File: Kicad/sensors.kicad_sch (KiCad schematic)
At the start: 13 parts, among them J5 Conn_02x03_Top_Bottom, J6 Conn_02x03_Top_Bottom, J7 Conn_02x03_Top_Bottom, J8 Conn_02x03_Top_Bottom, U1 ITR8307, U2 ITR8307, U3 ITR8307

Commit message: not small changes
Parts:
- removed J6, J7, J8: Conn_02x03_Top_Bottom, Connector_PinSocket_2.54mm:PinSocket_2x03_P2.54mm_Vertical, symbol Connector_Generic:Conn_02x03_Top_Bottom
- added TF2, TF3, TF4: Conn_02x03_Top_Bottom, Connector_PinHeader_2.54mm:PinHeader_2x03_P2.54mm_Vertical, symbol Connector_Generic:Conn_02x03_Top_Bottom
- TF1: renamed from J5; footprint Connector_PinSocket_2.54mm:PinSocket_2x03_P2.54mm_Vertical -> Connector_PinHeader_2.54mm:PinHeader_2x03_P2.54mm_Vertical
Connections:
- net +3.3V: now also TF1.2 (Pin_2), TF2.2 (Pin_2), TF3.2 (Pin_2), TF4.2 (Pin_2); no longer TF1.1 (Pin_1)
- net EXTI1: now also TF1.5 (Pin_5); no longer TF1.6 (Pin_6)
- net EXTI2: now also TF2.5 (Pin_5)
- net EXTI3: now also TF3.5 (Pin_5)
- net EXTI4: now also TF4.5 (Pin_5)
- net GND: now also TF1.4 (Pin_4), TF2.4 (Pin_4), TF3.4 (Pin_4), TF4.4 (Pin_4); no longer TF1.3 (Pin_3)
- net SCL1: now also TF1.3 (Pin_3), TF2.3 (Pin_3); no longer TF1.4 (Pin_4)
- net SCL2: now also TF3.3 (Pin_3), TF4.3 (Pin_3)
- net SDA1: now also TF1.6 (Pin_6), TF2.6 (Pin_6); no longer TF1.5 (Pin_5)
- net SDA2: now also TF3.6 (Pin_6), TF4.6 (Pin_6)
- net XSHUT1: now also TF1.1 (Pin_1); no longer TF1.2 (Pin_2)
- net XSHUT2: now also TF2.1 (Pin_1)
- net XSHUT3: now also TF3.1 (Pin_1)
- net XSHUT4: now also TF4.1 (Pin_1)
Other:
- moved on the sheet: TF1

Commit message: fixed scheme with i2c
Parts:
- renumbered TF1 to ToF1
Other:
- moved on the sheet: TF3
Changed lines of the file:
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@@
 	(wire
 		(pts
-			(xy 115.57 110.49) (xy 119.38 110.49)
+			(xy 118.11 110.49) (xy 121.92 110.49)
 		)
 		(stroke
@@
 	(wire
 		(pts
-			(xy 115.57 107.95) (xy 132.08 107.95)
+			(xy 118.11 107.95) (xy 134.62 107.95)
 		)
 		(stroke
@@
 	(wire
 		(pts
-			(xy 100.33 107.95) (xy 102.87 107.95)
+			(xy 102.87 107.95) (xy 105.41 107.95)
 		)
 		(stroke
@@
 	(wire
 		(pts
-			(xy 132.08 107.95) (xy 132.08 110.49)
+			(xy 134.62 107.95) (xy 134.62 110.49)
 		)
 		(stroke
@@
 	(wire
 		(pts
-			(xy 99.06 113.03) (xy 102.87 113.03)
+			(xy 101.6 113.03) (xy 105.41 113.03)
 		)
 		(stroke
@@
 	(wire
 		(pts
-			(xy 87.63 110.49) (xy 87.63 109.22)
+			(xy 90.17 110.49) (xy 90.17 109.22)
 		)
 		(stroke
@@
 	(wire
 		(pts
-			(xy 115.57 113.03) (xy 118.11 113.03)
+			(xy 118.11 113.03) (xy 120.65 113.03)
 		)
 		(stroke
@@
 	(wire
 		(pts
-			(xy 102.87 110.49) (xy 87.63 110.49)
+			(xy 105.41 110.49) (xy 90.17 110.49)
 		)
 		(stroke
@@
 	(hierarchical_label "SCL2"
 		(shape input)
-		(at 99.06 113.03 180)
+		(at 101.6 113.03 180)
 		(effects
 			(font
@@
 	(hierarchical_label "XSHUT3"
 		(shape input)
-		(at 100.33 107.95 180)
+		(at 102.87 107.95 180)
 		(effects
 			(font
@@
 	(hierarchical_label "EXTI3"
 		(shape input)
-		(at 119.38 110.49 0)
+		(at 121.92 110.49 0)
 		(effects
 			(font
@@
 	(hierarchical_label "SDA2"
 		(shape bidirectional)
-		(at 118.11 113.03 0)
+		(at 120.65 113.03 0)
 		(effects
 			(font
@@
 	(symbol
 		(lib_id "power:GND")
-		(at 132.08 110.49 0)
+		(at 134.62 110.49 0)
 		(unit 1)
 		(exclude_from_sim no)
@@
 		(fields_autoplaced yes)
 		(property "Reference" "#PWR063"
-			(at 132.08 116.84 0)
+			(at 134.62 116.84 0)
 			(effects
 				(font
@@
 		)
 		(property "Value" "GND"
-			(at 132.08 115.57 0)
+			(at 134.62 115.57 0)
 			(effects
 				(font
@@
 		)
 		(property "Footprint" ""
-			(at 132.08 110.49 0)
+			(at 134.62 110.49 0)
 			(effects
 				(font
@@
 		)
 		(property "Datasheet" ""
-			(at 132.08 110.49 0)
+			(at 134.62 110.49 0)
 			(effects
 				(font
@@
 		)
 		(property "Description" "Power symbol creates a global label with name \"GND\" , ground"
-			(at 132.08 110.49 0)
+			(at 134.62 110.49 0)
 			(effects
 				(font
@@
 	(symbol
 		(lib_id "power:+3.3V")
-		(at 87.63 109.22 0)
+		(at 90.17 109.22 0)
 		(unit 1)
 		(exclude_from_sim no)
@@
 		(fields_autoplaced yes)
 		(property "Reference" "#PWR062"
-			(at 87.63 113.03 0)
+			(at 90.17 113.03 0)
 			(effects
 				(font
@@
 		)
 		(property "Value" "+3.3V"
-			(at 87.63 104.14 0)
+			(at 90.17 104.14 0)
 			(effects
 				(font
@@
 		)
 		(property "Footprint" ""
-			(at 87.63 109.22 0)
+			(at 90.17 109.22 0)
 			(effects
 				(font
@@
 		)
 		(property "Datasheet" ""
-			(at 87.63 109.22 0)
+			(at 90.17 109.22 0)
 			(effects
 				(font
@@
 		)
 		(property "Description" "Power symbol creates a global label with name \"+3.3V\""
-			(at 87.63 109.22 0)
+			(at 90.17 109.22 0)
 			(effects
 				(font
@@
 		(dnp no)
 		(fields_autoplaced yes)
-		(property "Reference" "TF1"
+		(property "Reference" "ToF1"
 			(at 59.69 102.87 0)
 			(effects
@@
 			(project "MiniSumoSTM"
 				(path "/74ccf643-7ae0-4d9b-8b7c-e7e124cb3f26/07b86d8b-af43-4da9-8375-8e0423139cdc"
-					(reference "TF1")
+					(reference "ToF1")
 					(unit 1)
 				)
@@
 	(symbol
 		(lib_id "Connector_Generic:Conn_02x03_Top_Bottom")
-		(at 107.95 110.49 0)
+		(at 110.49 110.49 0)
 		(unit 1)
 		(exclude_from_sim no)
@@
 		(fields_autoplaced yes)
 		(property "Reference" "TF3"
-			(at 109.22 104.14 0)
+			(at 111.76 104.14 0)
 			(effects
 				(font
@@
 		)
 		(property "Value" "Conn_02x03_Top_Bottom"
-			(at 109.22 104.14 0)
+			(at 111.76 104.14 0)
 			(effects
 				(font
@@
 		)
 		(property "Footprint" "Connector_PinHeader_2.54mm:PinHeader_2x03_P2.54mm_Vertical"
-			(at 107.95 110.49 0)
+			(at 110.49 110.49 0)
 			(effects
 				(font
@@
 		)
 		(property "Datasheet" "~"
-			(at 107.95 110.49 0)
+			(at 110.49 110.49 0)
 			(effects
 				(font
@@
 		)
 		(property "Description" "Generic connector, double row, 02x03, top/bottom pin numbering scheme (row 1: 1...pins_per_row, row2: pins_per_row+1 ... num_pins), script generated (kicad-library-utils/schlib/autogen/connector/)"
-			(at 107.95 110.49 0)
-			(effects
-				(font
+			(at 110.49 110.49 0)
+			(effects
+				(font

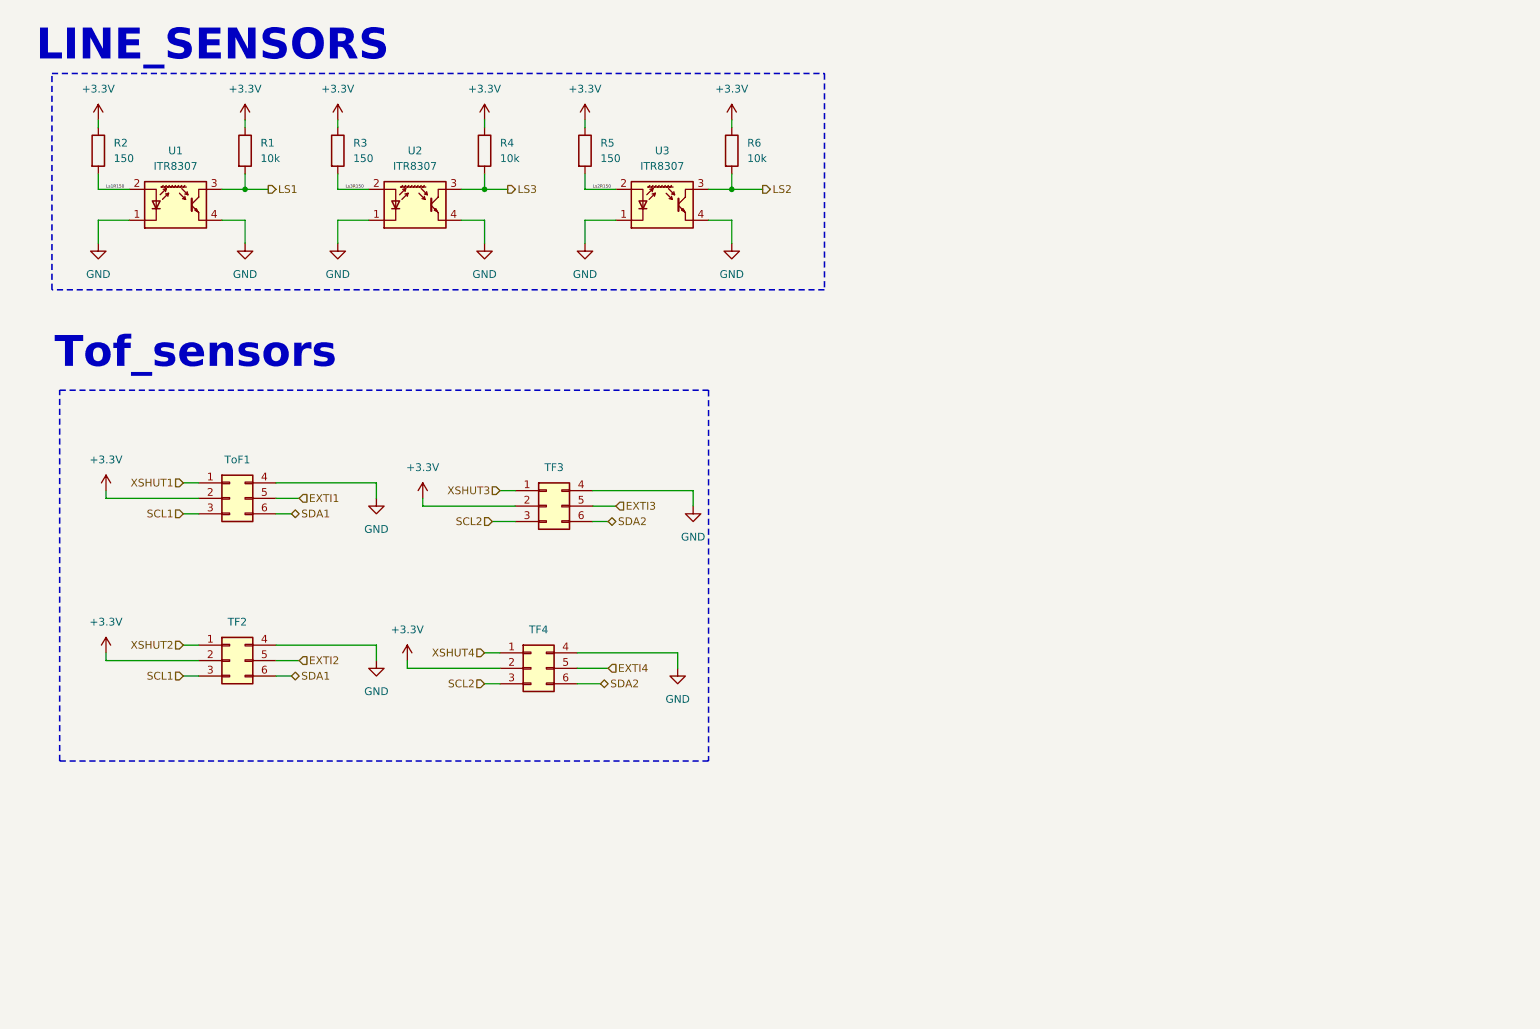
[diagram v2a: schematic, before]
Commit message: kicad schemas documentation
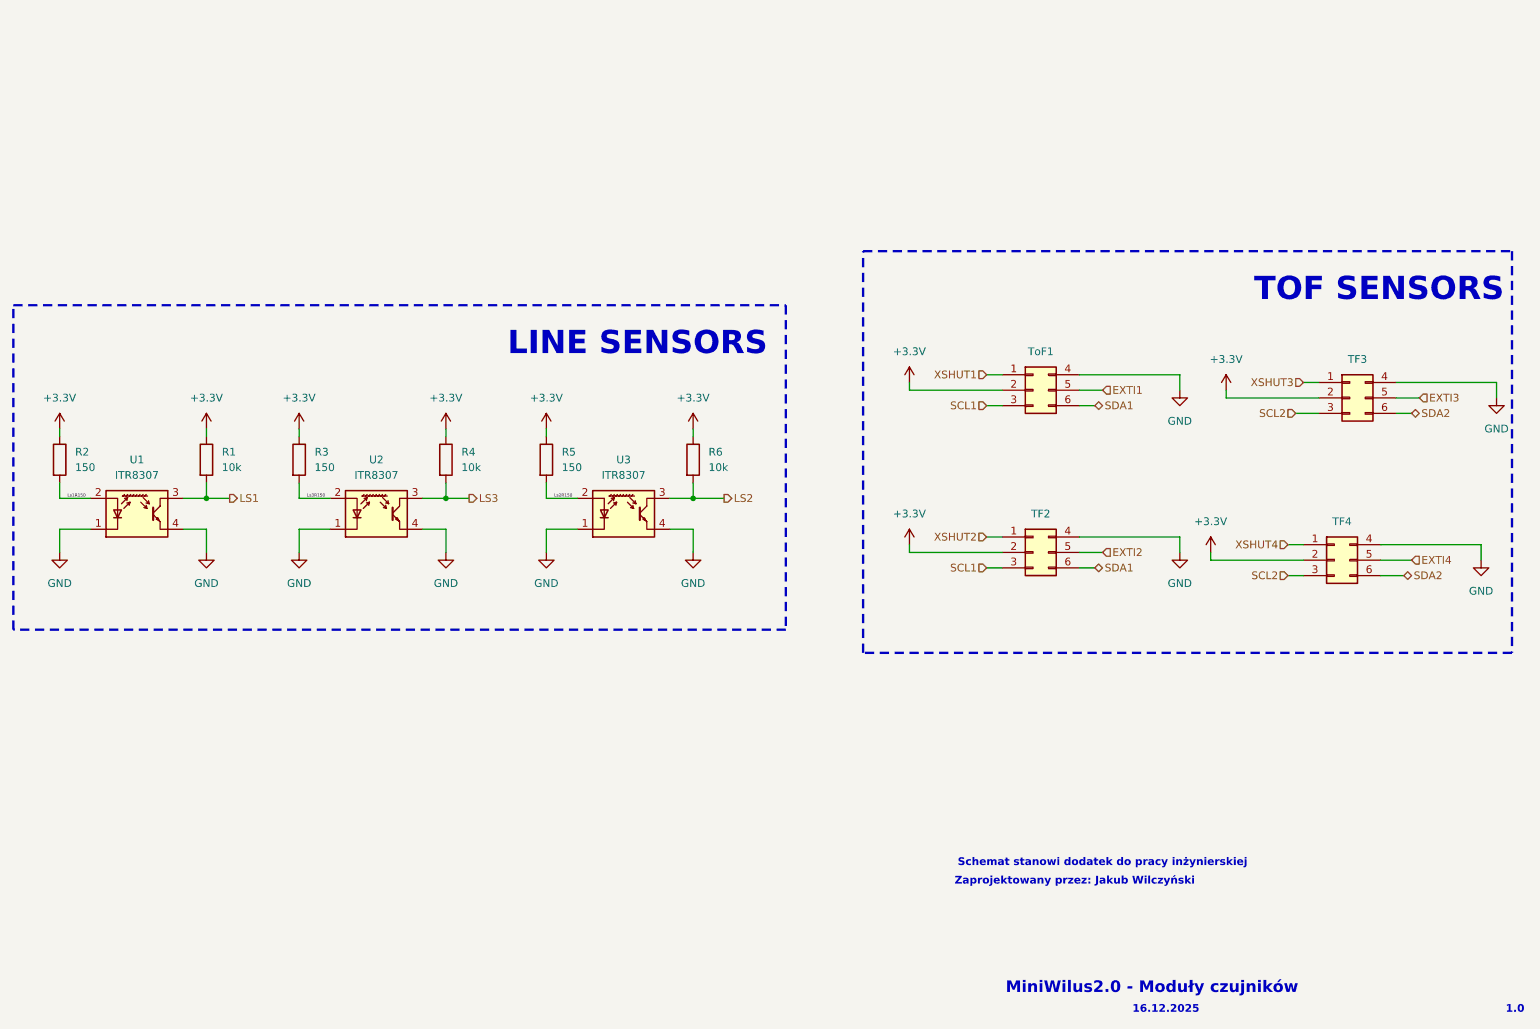
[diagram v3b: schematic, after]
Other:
- note added: "1.0"
- note added: "16.12.2025"
- note added: "LINE SENSORS"
- note added: "MiniWilus2.0 - Moduły czujników"
- note added: "Schemat stanowi dodatek do pracy inżynierskiej"
- note added: "TOF SENSORS"
- note added: "Zaprojektowany przez: Jakub Wilczyński"
- note removed: "LINE_SENSORS"
- note removed: "Tof_sensors"
- moved on the sheet: R1, R2, R3, R4, R5, R6, TF2, TF3, TF4, ToF1, U1, U2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
